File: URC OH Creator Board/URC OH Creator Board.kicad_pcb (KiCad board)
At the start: 2 copper layers, 80 x 53.5 mm, 21 parts, among them J1 Conn_01x20_Pin, J10 Conn_01x20_Pin, J11 Conn_01x20_Pin, J12 Conn_01x20_Pin, J2 Conn_01x20_Pin, J3 Conn_01x20_Pin, J4 Conn_01x20_Pin, J5 Conn_01x20_Pin, J6 Conn_01x20_Pin, J7 Conn_01x20_Pin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

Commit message: added board edge locks
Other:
- board text added: "Front panel thickness"
- board text added: "Rear board edge can extend back further"
- board text added: "Suggested placement of Serial Funcion switch"
- board text added: "locked"
- board text removed: "Copyright (c) 2024 G1LRO"
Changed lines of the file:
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@@
     )
   )
-  (footprint "URCEXTRAS:SW_TPDT_THT-5mm" (layer "F.Cu")
+  (footprint "URCEXTRAS:SW_TPDT_THT-5mm" locked (layer "F.Cu")
     (at 68.275 146.65)
     (descr "Sub-miniature slide switch, right-angle, https://datasheet.lcsc.com/lcsc/1912111437_SHOU-HAN-SK13D07VG5_C393948.pdf")
@@
     (fp_rect (start -1 2.3) (end 1 7.3)
       (stroke (width 0.1) (type default)) (fill none) (layer "F.Fab"))
-    (pad "" thru_hole oval (at -6.15 0) (size 1 1.9) (drill oval 0.5 1.4) (layers "*.Cu" "*.Mask"))
-    (pad "" thru_hole oval (at 6.15 0) (size 1 1.9) (drill oval 0.5 1.4) (layers "*.Cu" "*.Mask"))
-    (pad "1" thru_hole circle (at -4 0) (size 1.1 1.1) (drill 0.6) (layers "*.Cu" "*.Mask")
+    (pad "" thru_hole oval locked (at -6.15 0) (size 1 1.9) (drill oval 0.5 1.4) (layers "*.Cu" "*.Mask"))
+    (pad "" thru_hole oval locked (at 6.15 0) (size 1 1.9) (drill oval 0.5 1.4) (layers "*.Cu" "*.Mask"))
+    (pad "1" thru_hole circle locked (at -4 0) (size 1.1 1.1) (drill 0.6) (layers "*.Cu" "*.Mask")
       (net 57 "Net-(RXD->CPU1-Pad1)") (pinfunction "1") (pintype "passive"))
-    (pad "2" thru_hole circle (at 2 0) (size 1.11 1.11) (drill 0.6) (layers "*.Cu" "*.Mask")
+    (pad "2" thru_hole circle locked (at 2 0) (size 1.11 1.11) (drill 0.6) (layers "*.Cu" "*.Mask")
       (net 4 "CAT TO AIOC-RXD") (pinfunction "2") (pintype "passive"))
-    (pad "3" thru_hole circle (at 0 0) (size 1.1 1.1) (drill 0.6) (layers "*.Cu" "*.Mask")
+    (pad "3" thru_hole circle locked (at 0 0) (size 1.1 1.1) (drill 0.6) (layers "*.Cu" "*.Mask")
       (net 3 "AIOC RXD") (pinfunction "3") (pintype "passive"))
-    (pad "4" thru_hole circle (at 4 0) (size 1.1 1.1) (drill 0.6) (layers "*.Cu" "*.Mask")
+    (pad "4" thru_hole circle locked (at 4 0) (size 1.1 1.1) (drill 0.6) (layers "*.Cu" "*.Mask")
       (net 5 "HT TO AIOC-RXD") (pinfunction "4") (pintype "passive"))
     (model "${KICAD6_3DMODEL_DIR}/Button_Switch_SMD.3dshapes/SW_SPDT_CK-JS102011SAQN.wrl"
@@
       (net 1 "GND") (pinfunction "1") (pintype "passive"))
   )
-  (footprint "Symbol:OSHW-Logo2_9.8x8mm_SilkScreen" (layer "B.Cu")
+  (footprint "Symbol:OSHW-Logo2_9.8x8mm_SilkScreen" locked (layer "B.Cu")
     (at 123 146 180)
     (descr "Open Source Hardware Symbol")
@@
   (gr_rect (start 128.45 150.05) (end 136.45 152.15)
     (stroke (width 0.2) (type default)) (fill none) (layer "Dwgs.User"))
-  (gr_line (start 140 105.725) (end 140 98)
+  (gr_line locked (start 140 105.725) (end 140 98)
     (stroke (width 0.1) (type default)) (layer "Edge.Cuts"))
-  (gr_line (start 60 140.675) (end 60 150)
+  (gr_line locked (start 60 140.675) (end 60 150)
     (stroke (width 0.1) (type default)) (layer "Edge.Cuts"))
-  (gr_line (start 140 96.5) (end 140 98)
+  (gr_line locked (start 140 96.5) (end 140 98)
     (stroke (width 0.1) (type default)) (layer "Edge.Cuts"))
-  (gr_line (start 60 105.55) (end 60 98)
+  (gr_line locked (start 60 105.55) (end 60 98)
     (stroke (width 0.1) (type default)) (layer "Edge.Cuts"))
   (gr_line (start 60 96.5) (end 140 96.5)
     (stroke (width 0.1) (type default)) (layer "Edge.Cuts"))
-  (gr_line (start 60 96.5) (end 60 98)
+  (gr_line locked (start 60 96.5) (end 60 98)
     (stroke (width 0.1) (type default)) (layer "Edge.Cuts"))
-  (gr_line (start 60 105.55) (end 60 140.675)
+  (gr_line locked (start 60 105.55) (end 60 140.675)
     (stroke (width 0.1) (type default)) (layer "Edge.Cuts"))
-  (gr_line (start 140 150) (end 60 150)
+  (gr_line locked (start 140 150) (end 60 150)
     (stroke (width 0.1) (type default)) (layer "Edge.Cuts"))
-  (gr_line (start 140 105.725) (end 140 140.725)
+  (gr_line locked (start 140 105.725) (end 140 140.725)
     (stroke (width 0.1) (type default)) (layer "Edge.Cuts"))
-  (gr_line (start 140 150) (end 140 140.725)
+  (gr_line locked (start 140 150) (end 140 140.725)
     (stroke (width 0.1) (type default)) (layer "Edge.Cuts"))
-  (gr_text "Copyright (c)\n 2024 G1LRO" (at 133.3 149.1) (layer "B.SilkS")
+  (gr_text locked "Copyright (c)\n 2024 G1LRO" (at 133.3 149.1) (layer "B.SilkS")
     (effects (font (size 1 1) (thickness 0.15)) (justify bottom mirror))
   )
@@
     (effects (font (size 1.5 1.5) (thickness 0.3) bold) (justify left bottom))
   )
+  (gr_text "Front panel thickness" (at 75.6 152) (layer "Cmts.User")
+    (effects (font (size 1 1) (thickness 0.15)) (justify left bottom))
+  )
+  (gr_text "Suggested placement\nof Serial Funcion switch" (at 41.6 148.3) (layer "Cmts.User")
+    (effects (font (size 1 1) (thickness 0.15)) (justify left bottom))
+  )
+  (gr_text "Rear board edge can extend back further" (at 72.4 96) (layer "Cmts.User")
+    (effects (font (size 1 1) (thickness 0.15)) (justify left bottom))
+  )
   (segment (start 62.125 146.65) (end 62.125 147.425) (width 0.25) (layer "F.Cu") (net 1))

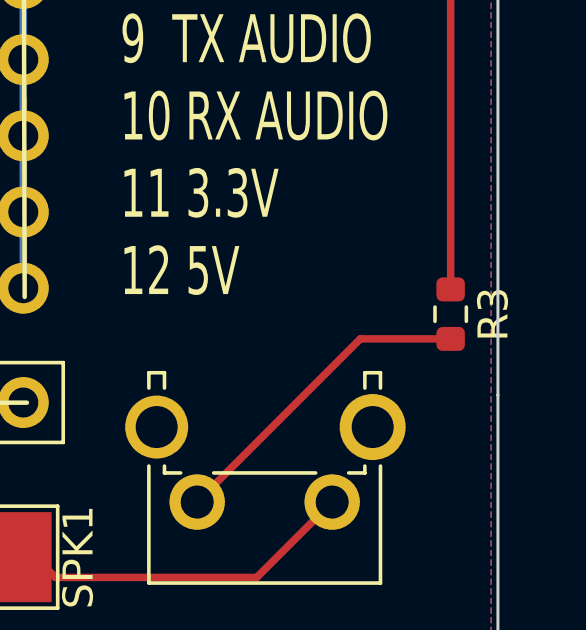
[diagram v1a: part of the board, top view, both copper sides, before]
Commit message: Changed speaker series resistor to 10uF capacitor
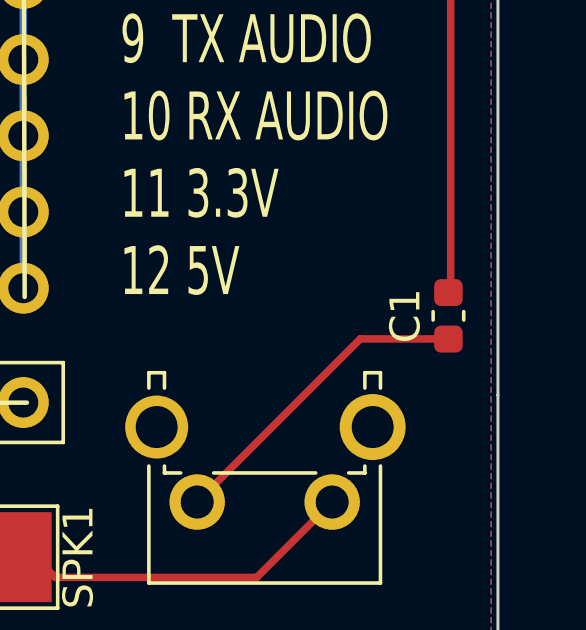
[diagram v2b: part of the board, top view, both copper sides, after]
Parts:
- removed R3: 22R, Resistor_SMD:R_0603_1608Metric
- added C1: 10u/10V/X5R, Capacitor_SMD:C_0603_1608Metric, F.Cu at (138.3, 138.1)
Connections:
- SW1 pad : (no net) -> GND
